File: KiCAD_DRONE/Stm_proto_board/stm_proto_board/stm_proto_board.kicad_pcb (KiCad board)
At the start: 2 copper layers, 33 x 83.8 mm, 3 parts, among them J1 Conn_01x32, J2 Conn_01x32, U1 STM32F103R(C-D-E)Tx

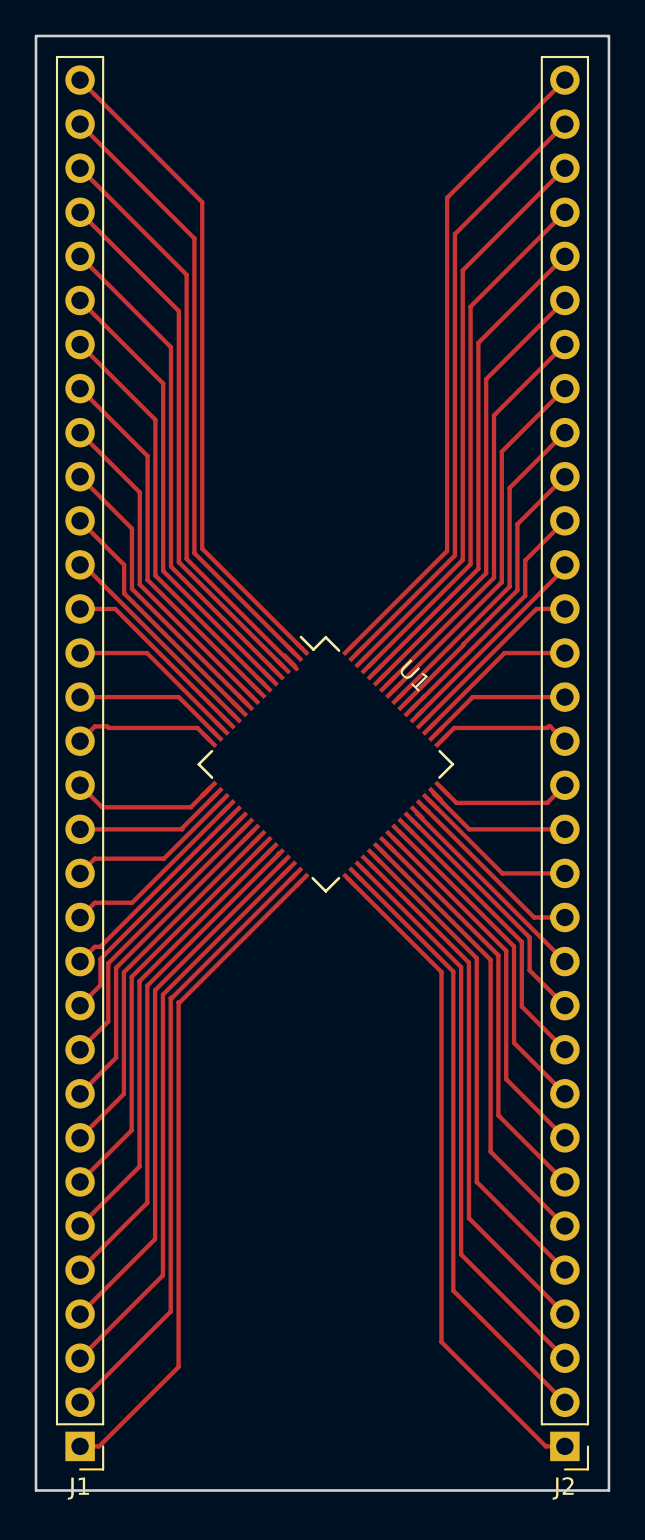
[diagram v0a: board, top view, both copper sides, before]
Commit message: added the m60 files for the stm proto board and the gate driver IC. updated code to drive motor. not sure if it works or not.
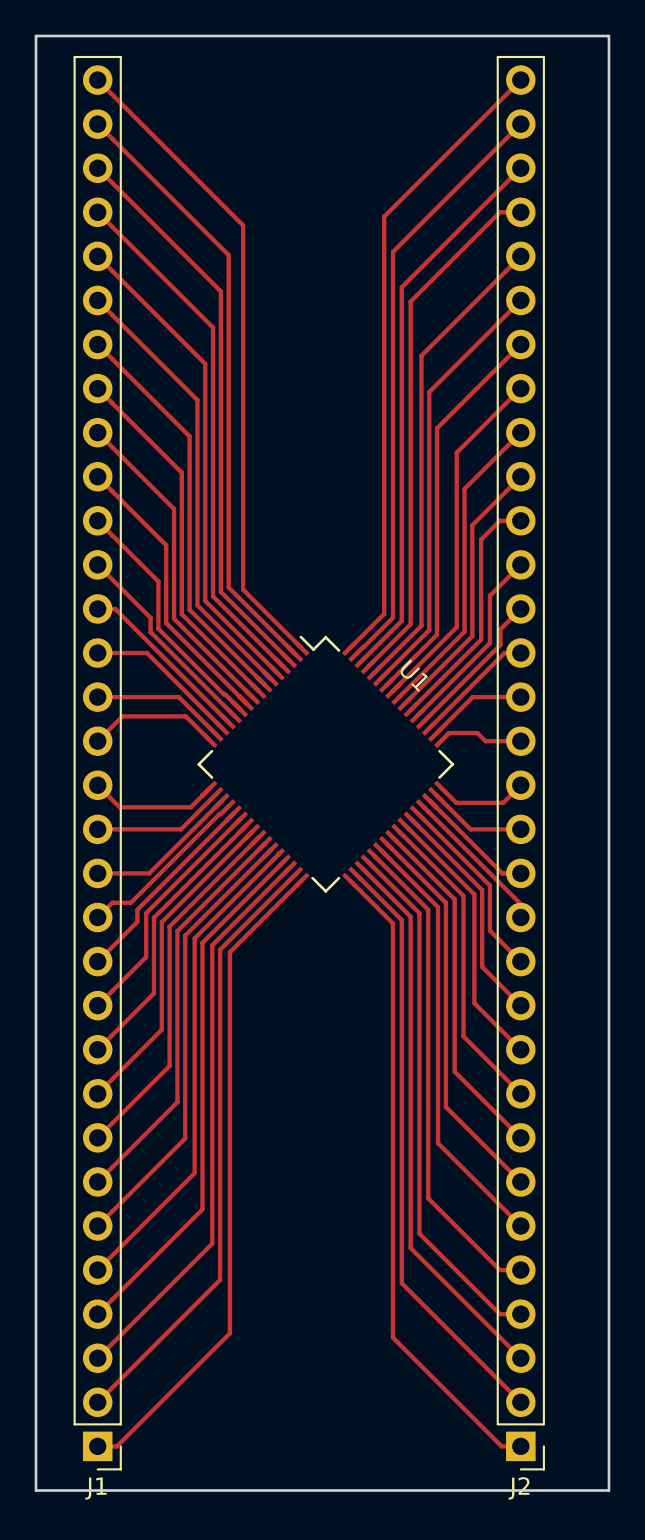
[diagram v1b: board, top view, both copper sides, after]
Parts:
- moved J2 2.54 mm to (160.0, 125.7)
- moved J1 1.02 mm to (135.6, 125.7)
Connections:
- J2 pad 32: Net-(J1-Pad20) -> Net-(J2-Pad32)
- U1 pad 64: Net-(J1-Pad20) -> Net-(J2-Pad32)
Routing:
- net Net-(J1-Pad20): track 49.1 -> 10.2 mm
- net Net-(J2-Pad32): track 0.00 -> 36.8 mm
- net Net-(J2-Pad17): track 7.78 -> 4.93 mm
- net Net-(J2-Pad15): track 8.44 -> 5.75 mm
- net Net-(J2-Pad16): track 7.87 -> 5.33 mm
- net Net-(J2-Pad19): track 9.60 -> 7.06 mm
- net Net-(J2-Pad18): track 8.34 -> 5.80 mm
- net Net-(J2-Pad13): track 10.8 -> 8.71 mm
- net Net-(J2-Pad20): track 10.9 -> 8.84 mm
- net Net-(J2-Pad14): track 9.54 -> 7.60 mm
- net Net-(J2-Pad1): track 38.6 -> 37.4 mm
- net Net-(J1-Pad30): track 34.0 -> 33.0 mm
- net Net-(J1-Pad15): track 8.71 -> 7.65 mm
- net Net-(J2-Pad23): track 16.9 -> 15.8 mm
- net Net-(J2-Pad8): track 21.4 -> 20.4 mm
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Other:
- rule trace_min: 0.2 -> 0.254
